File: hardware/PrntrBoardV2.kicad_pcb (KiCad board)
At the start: 2 copper layers, 148.7 x 104.3 mm, 248 parts, among them J10 Conn_01x03_Male, J11 Conn_01x03_Male, J12 Conn_01x03_Male, J13 Conn_01x03_Male, J14 Conn_01x03_Male, J15 Conn_01x03_Male, J16 JST XH, J17 KF350, J18 JST XH, J19 JST XH, J20 KF350, J21 JST XH, J3 USB_B_Micro, J4 JST XH, J5 KF129, J6 KF350, J7 Conn_01x03_Male, J8 Conn_01x03_Male, J9 Conn_01x03_Male, U1 74LVC125, U2 STM32F407VETx, U3 24LC64, U4 AMS1117-3.3, U5 DCBuck, U6 74HCT02, Y1 8MHz

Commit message: 40 unrouted traces.
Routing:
- net ~X_MIN: track 0.00 -> 136.5 mm, vias 0 -> 7
- net ~Y_MIN: track 0.00 -> 108.9 mm, vias 0 -> 6
- net ~Z_MAX: track 57.2 -> 148.4 mm, vias 2 -> 6
- net ~Z_MIN: track 45.9 -> 118.4 mm, vias 2 -> 4
- net /Sheet5DABBBAA/SPI1_MOSI_CPU: track 0.00 -> 52.7 mm, vias 0 -> 2
- net ~RESET: track 97.2 -> 138.0 mm
- net SPI1_MISO: track 154.2 -> 175.7 mm, vias 1 -> 2
- net LCD_RS: track 61.4 -> 63.1 mm
- net ~LCD_E: track 56.9 -> 58.5 mm
- net LCD_D6: track 67.0 -> 68.2 mm
- net LCD_D7: track 62.8 -> 63.9 mm
- net ~X_MAX: track 60.1 -> 59.1 mm
- net BEEP: track 65.7 -> 66.5 mm
- net LCD_D4: track 67.6 -> 68.4 mm
- net ADC5: track 96.9 -> 97.4 mm
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
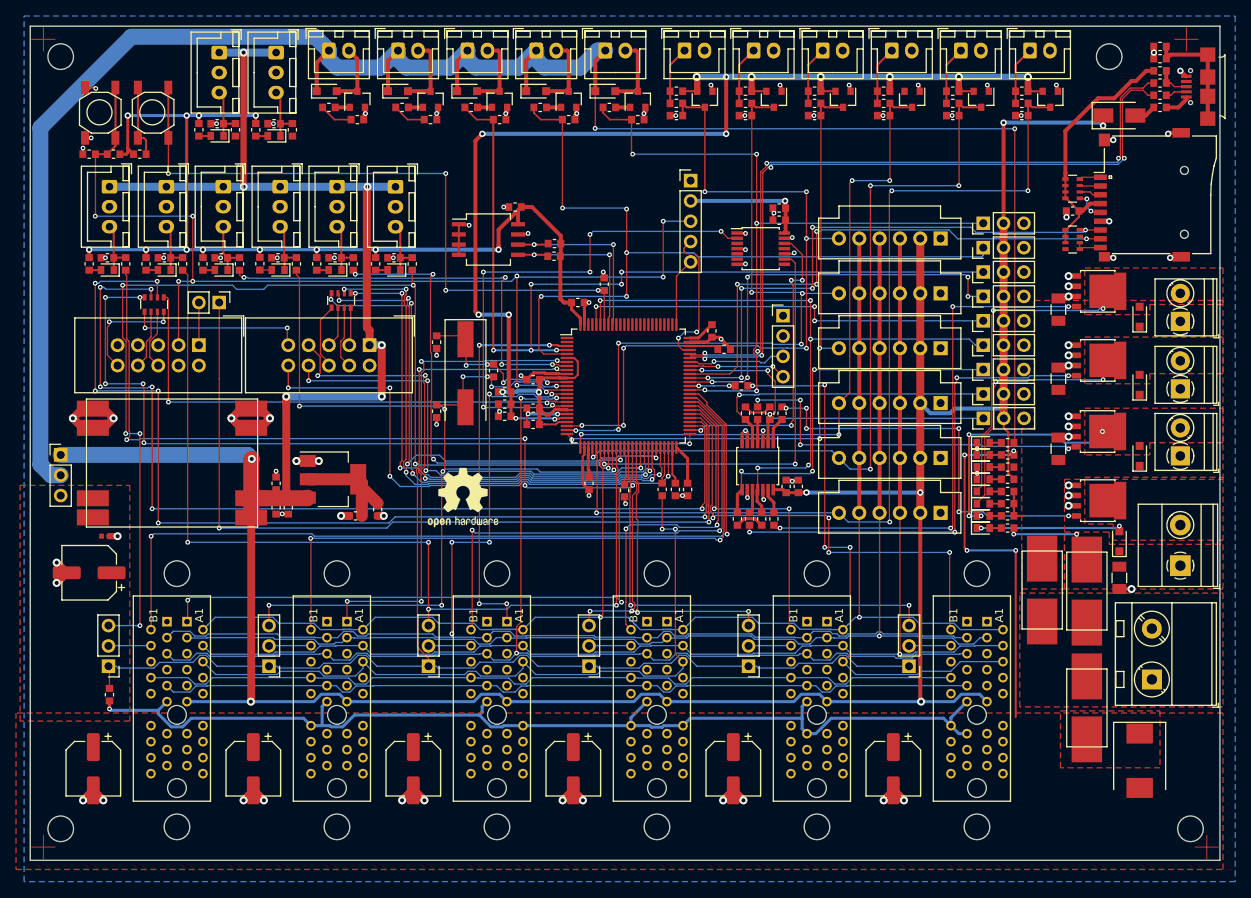
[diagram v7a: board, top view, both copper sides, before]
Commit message: 15 unrouted traces.
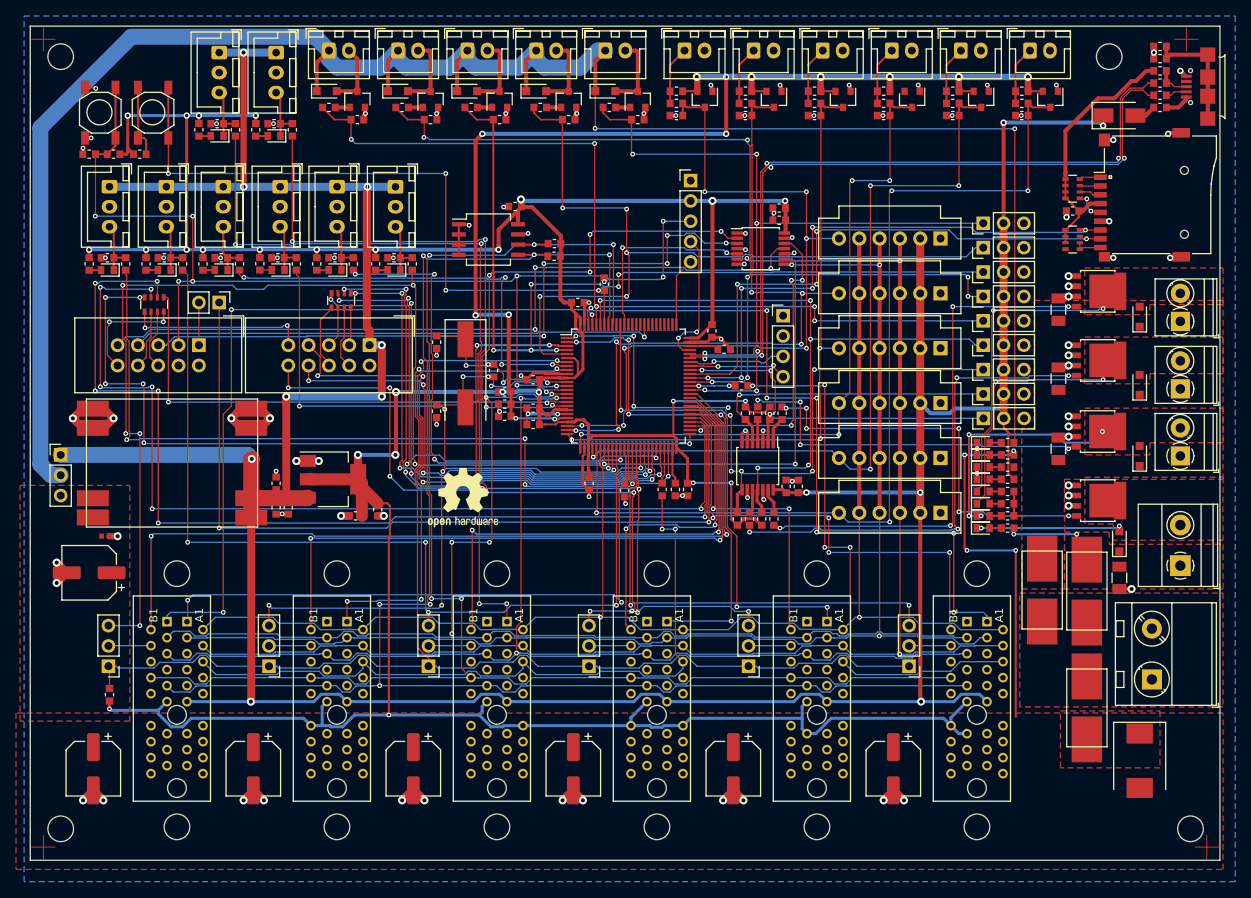
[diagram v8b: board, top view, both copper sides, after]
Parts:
- moved C11 0.06 mm to (83.7, 81.7)
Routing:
- net 3.3V: track 368.3 -> 516.2 mm, vias 16 -> 26
- net ~V_MIN: track 36.7 -> 132.3 mm, vias 2 -> 6
- net SPI2_SCK: track 0.00 -> 94.1 mm, vias 0 -> 3
- net ST1_STEP: track 0.00 -> 92.8 mm, vias 0 -> 3
- net ~ST6_CS: track 0.00 -> 90.5 mm, vias 0 -> 7
- net ~U_MIN: track 28.2 -> 116.5 mm, vias 2 -> 6
- net SPI2_MOSI: track 0.00 -> 86.1 mm, vias 0 -> 5
- net I2C_SDA: track 125.3 -> 200.2 mm, vias 2 -> 6
- net I2C_SCL: track 127.1 -> 198.1 mm, vias 2 -> 5
- net ~ST5_CS: track 0.00 -> 67.9 mm, vias 0 -> 6
- net ~SD_DETECT: track 0.00 -> 65.8 mm, vias 0 -> 1
- net ~ST4_CS: track 0.00 -> 63.3 mm, vias 0 -> 5
- net PWM6: track 56.3 -> 116.7 mm, vias 5 -> 7
- net PWM5: track 56.6 -> 110.2 mm, vias 3 -> 5
- net PWM3: track 48.5 -> 81.5 mm, vias 3 -> 6
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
